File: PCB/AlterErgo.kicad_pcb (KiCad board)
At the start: 2 copper layers, 104 parts, among them J1 GS3, J2 SJ-43514, J3 GS3, J4 Conn_01x02, SW0:10 SW_Push, SW0:11 SW_Push, SW0:12 SW_Push, SW0:7 SW_Push, SW0:8 SW_Push, SW0:9 SW_Push, SW1 SW_SPST, SW1:10 SW_Push, SW1:11 SW_Push, SW1:12 SW_Push, SW1:13 SW_Push, SW1:7 SW_Push, SW1:8 SW_Push, SW1:9 SW_Push, SW2:10 SW_Push, SW2:11 SW_Push, SW2:12 SW_Push, SW2:13 SW_Push, SW2:7 SW_Push, SW2:8 SW_Push, SW2:9 SW_Push, SW3:10 SW_Push, SW3:11 SW_Push, SW3:12 SW_Push, SW3:13 SW_Push, SW3:8 SW_Push, SW3:9 SW_Push, SW4:10 SW_Push, SW4:11 SW_Push, SW4:12 SW_Push, SW4:13 SW_Push, SW4:7 SW_Push, SW4:8 SW_Push, SW4:9 SW_Push, SW5:10 SW_Push, SW5:11 SW_Push, SW5:12 SW_Push, SW5:13 SW_Push, SW5:7 SW_Push, SW5:8 SW_Push, SW5:9 SW_Push, U1 Feather32u4Bluefruit, U2 MCP23018

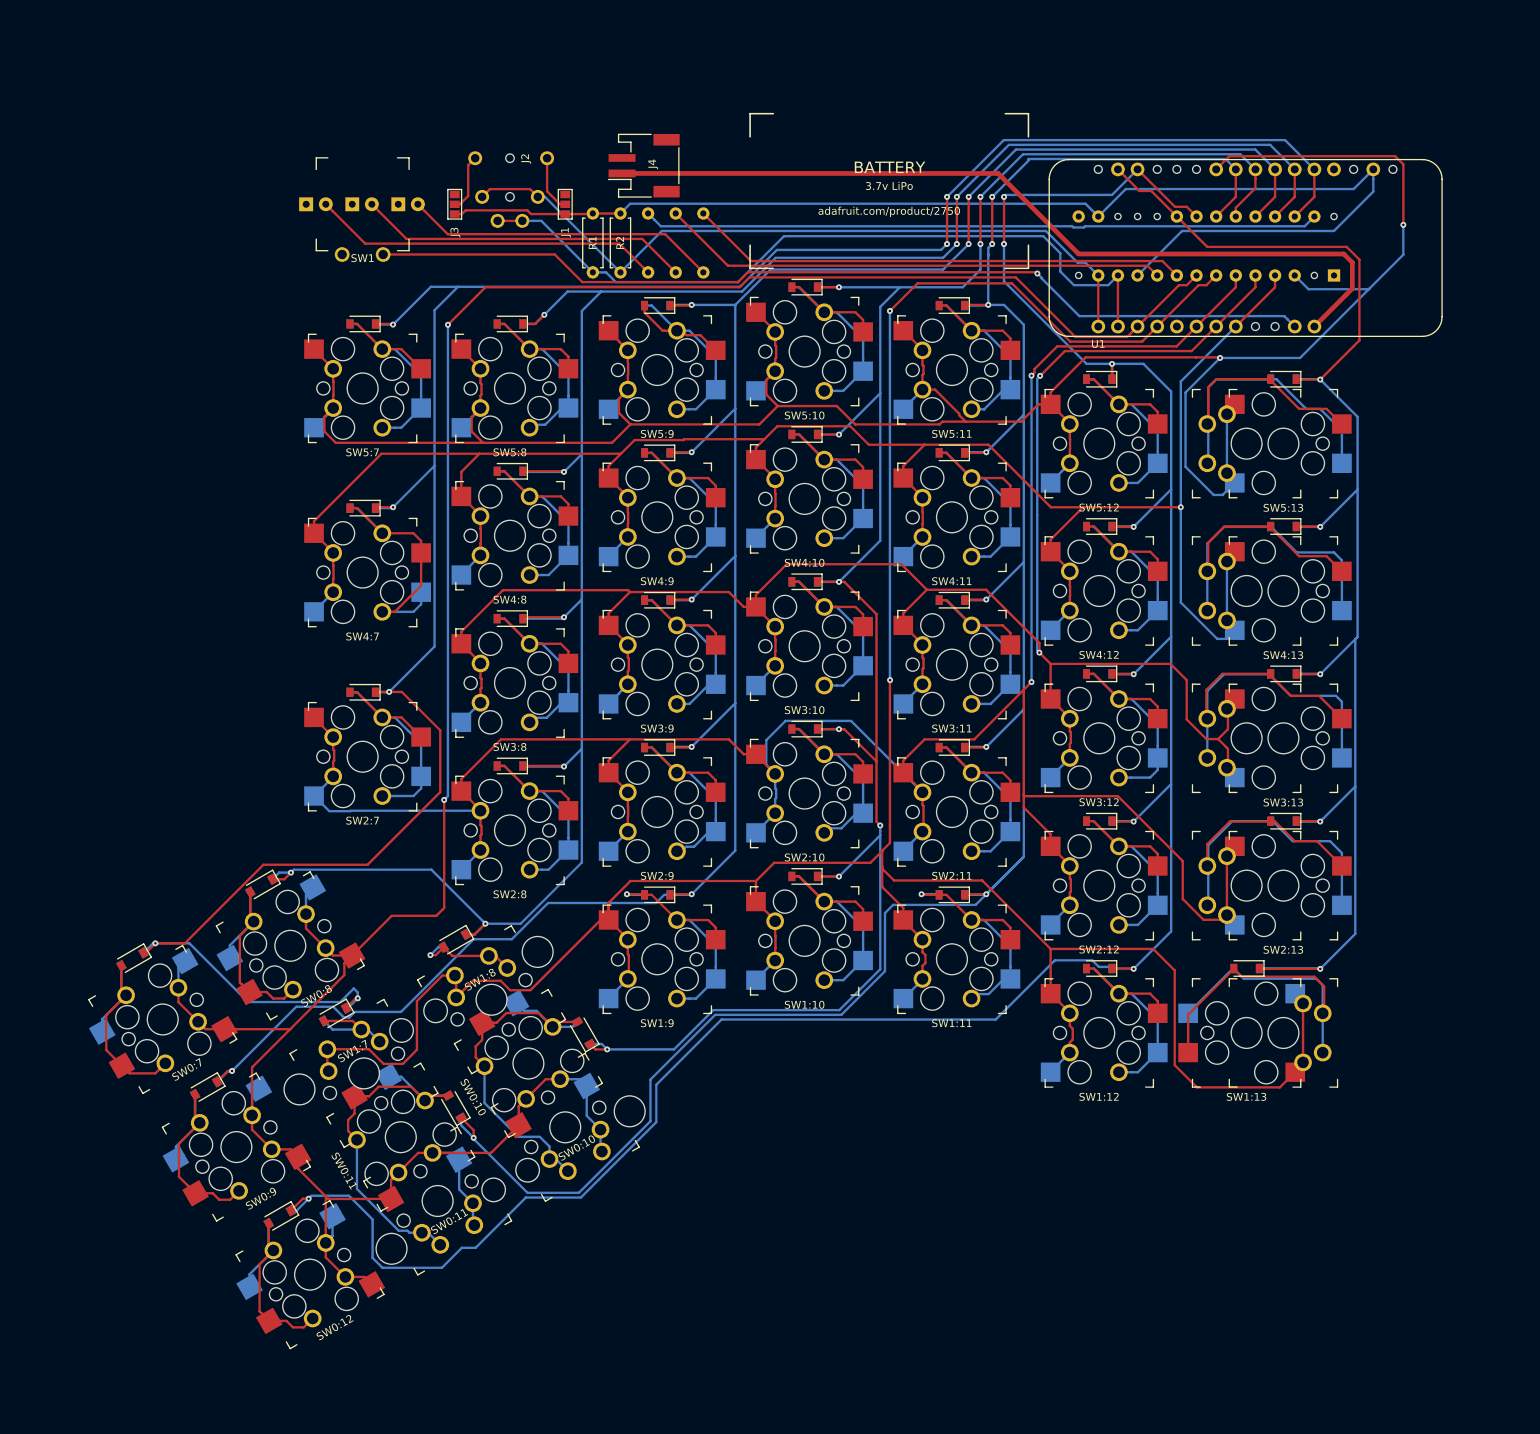
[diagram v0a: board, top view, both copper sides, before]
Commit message: Accept through hole or surface mount 1N4148 diodes; clean up some routing slightly
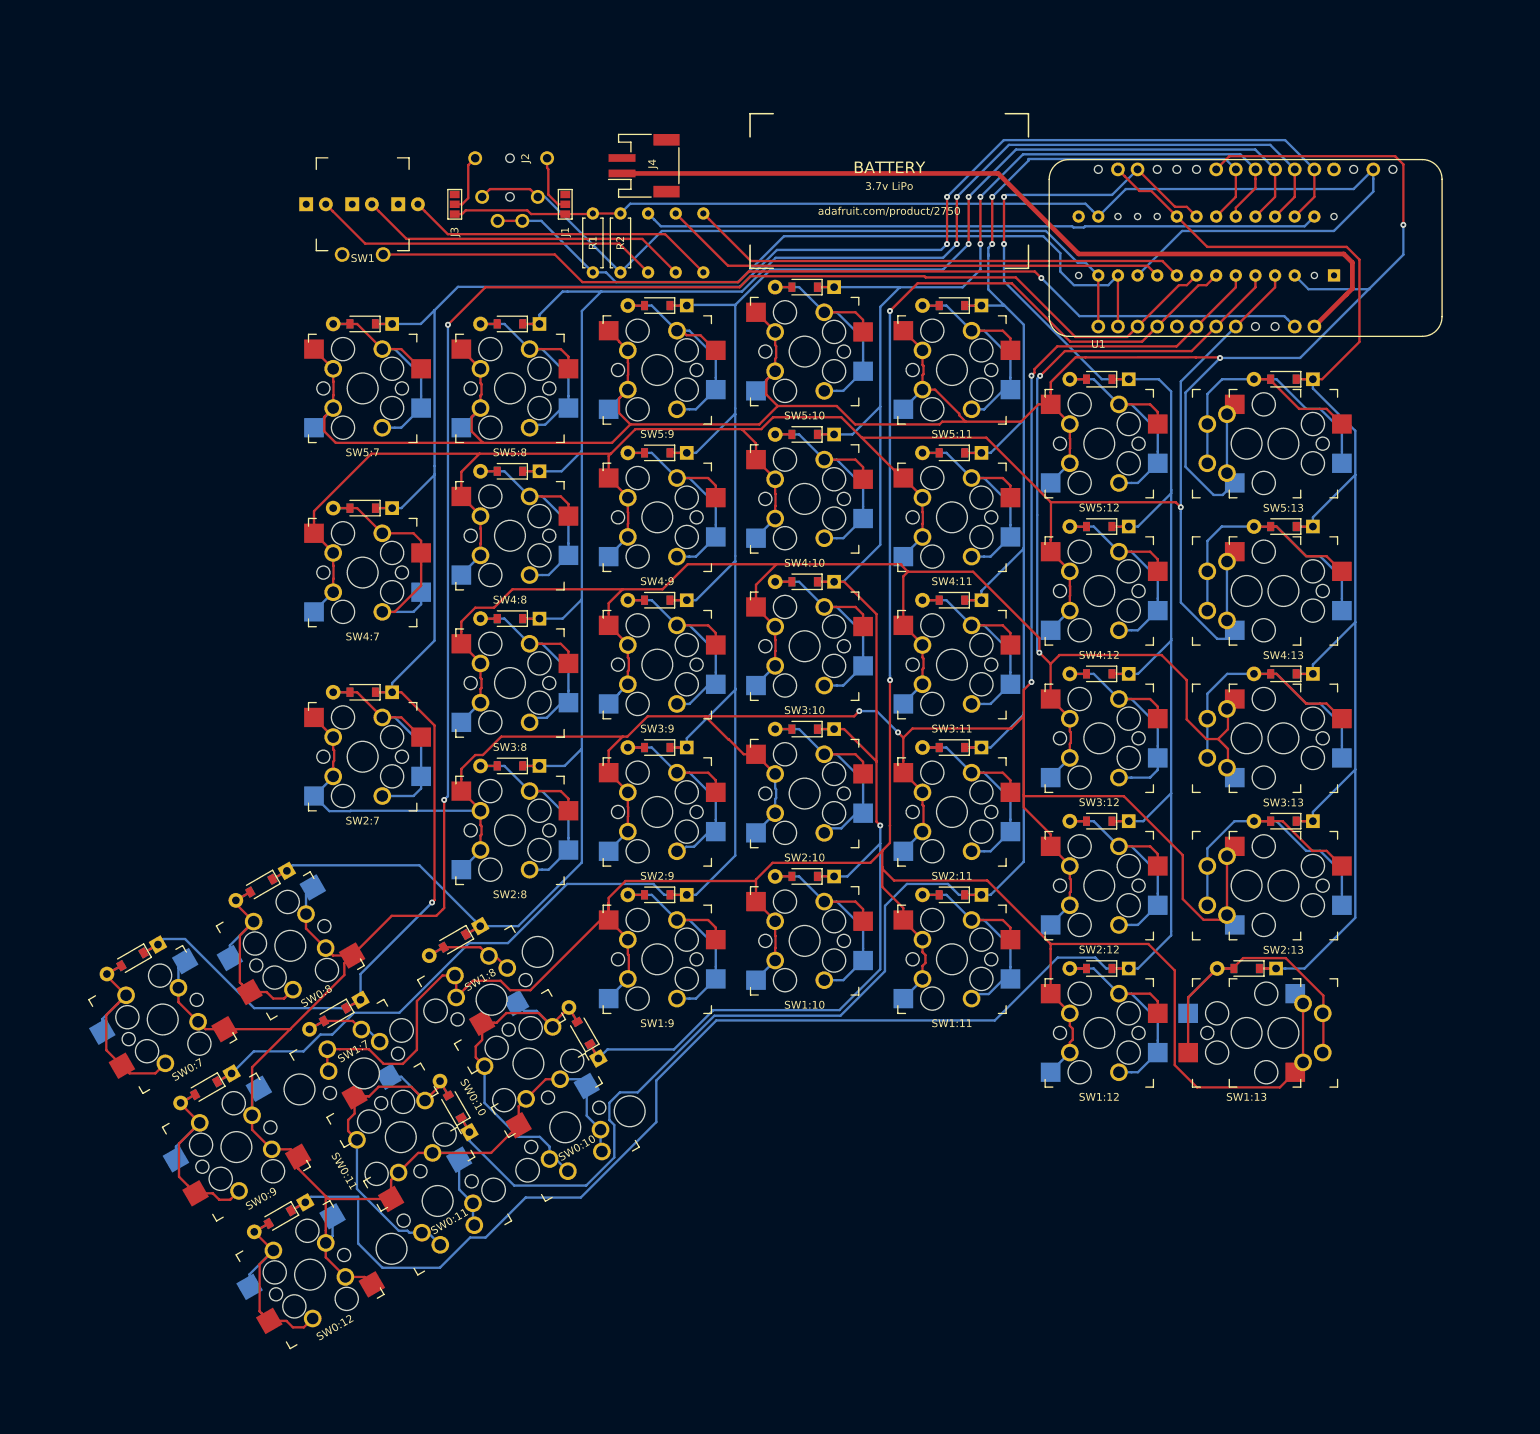
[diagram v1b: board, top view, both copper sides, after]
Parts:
- D0:10, D0:11, D0:12, D0:7, D0:8, D0:9, D1:10, D1:11, D1:12, D1:13, D1:7, D1:8, D1:9, D2:10, D2:11, D2:12, D2:13, D2:7, D2:8, D2:9, D3:10, D3:11, D3:12, D3:13, D3:8, D3:9, D4:10, D4:11, D4:12, D4:13, D4:7, D4:8, D4:9, D5:10, D5:11, D5:12, D5:13, D5:7, D5:8, D5:9: footprint keyboard_accessories:D_SOD-123_2sided_hiddenlabel -> keyboard_accessories:D_SOD-123_2sided_DO-35_combo
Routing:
- net /COL6: track 318.6 -> 297.8 mm, vias 7 -> 3
- net Net-(D1:13-Pad2): track 59.3 -> 46.0 mm
- net Net-(D3:13-Pad2): track 60.4 -> 48.2 mm
- net Net-(D4:13-Pad2): track 60.0 -> 48.3 mm
- net /COL5: track 297.4 -> 285.8 mm, vias 8 -> 2
- net Net-(D2:13-Pad2): track 58.8 -> 47.4 mm
- net Net-(D5:13-Pad2): track 59.1 -> 48.3 mm
- net /COL11: track 292.7 -> 284.4 mm, vias 8 -> 2
- net /ROW3: track 276.8 -> 284.2 mm
- net /COL0: track 194.8 -> 188.4 mm, vias 5 -> 0
- net /ROW4: track 279.7 -> 283.5 mm
- net /COL1: track 327.5 -> 323.8 mm, vias 8 -> 2
- net Net-(D0:11-Pad2): track 49.5 -> 52.4 mm
- net /COL10: track 262.8 -> 260.4 mm, vias 9 -> 3
- net Net-(D0:12-Pad2): track 30.3 -> 32.3 mm
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
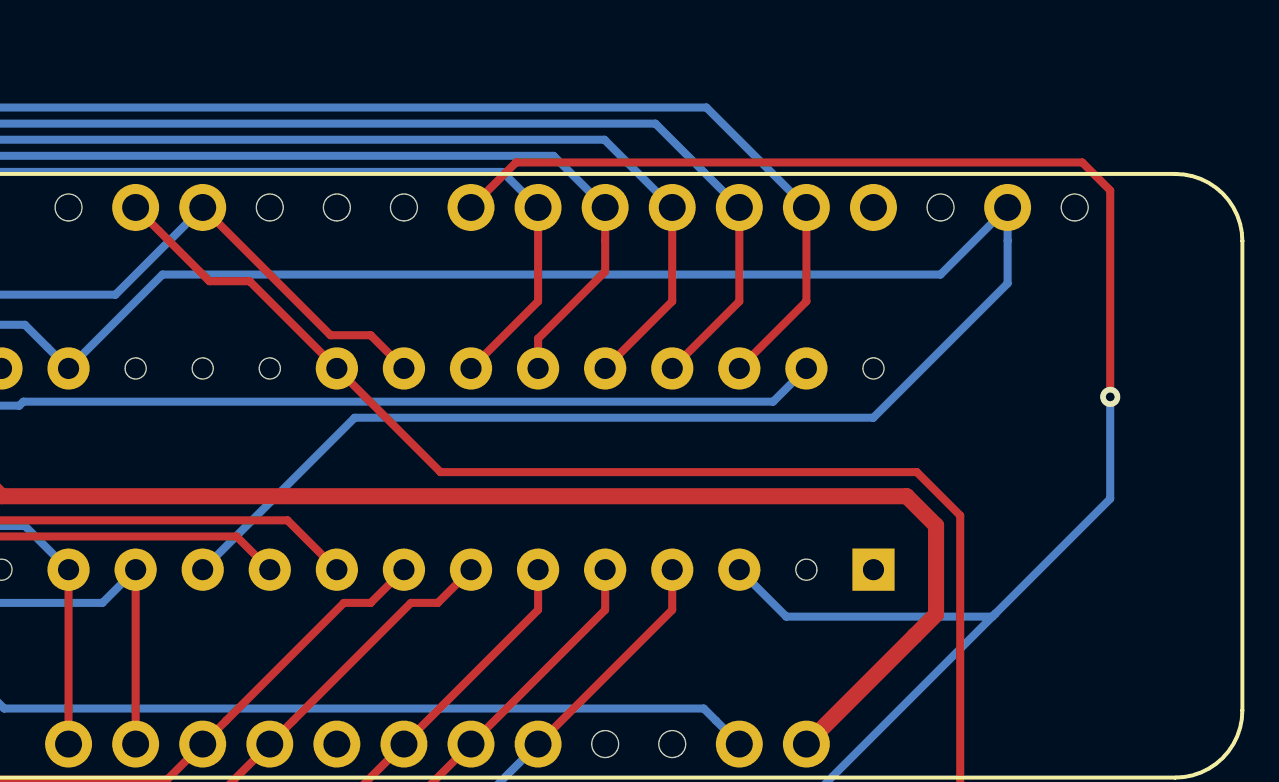
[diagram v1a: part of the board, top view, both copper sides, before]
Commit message: Add hole to allow Feather reset button to be pressed even when installed upside-down on the left-hand PCB
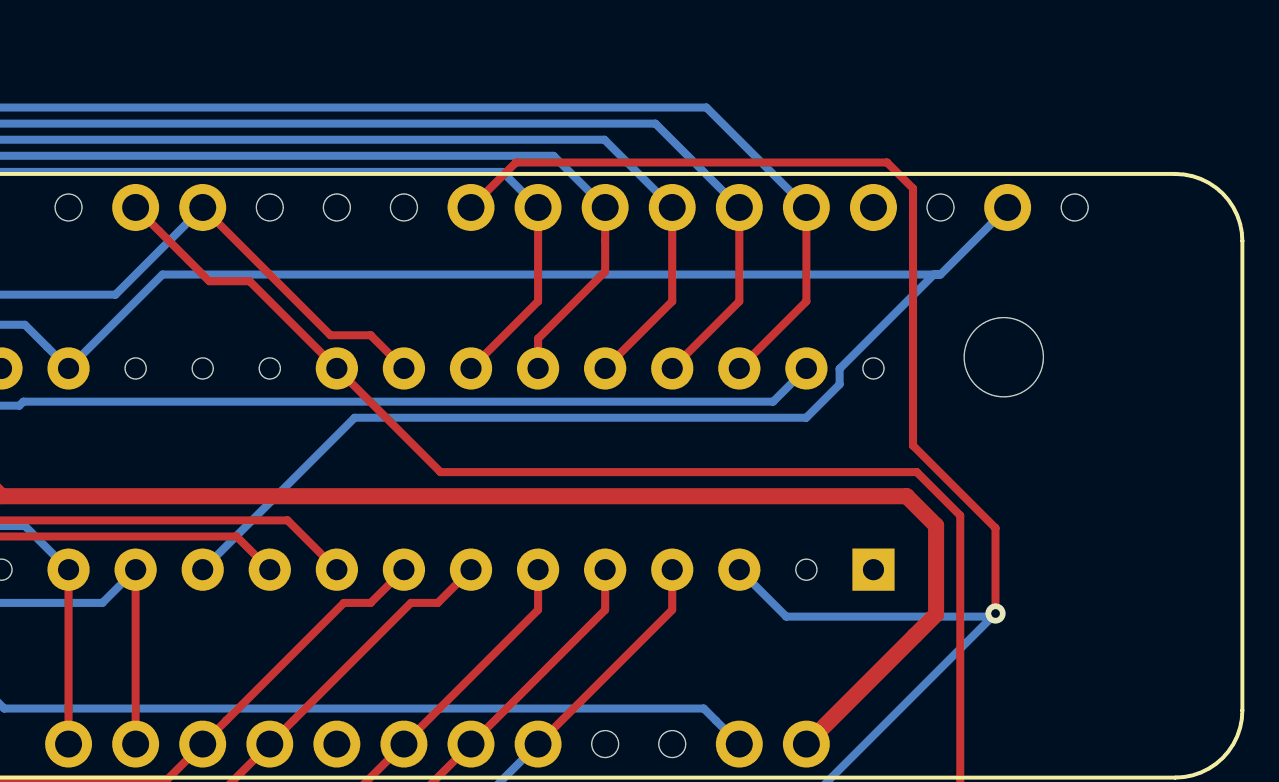
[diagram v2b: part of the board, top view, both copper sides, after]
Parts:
- added RESET: ResetHole, Mounting_Holes:MountingHole_3mm, F.Cu at (211.5, 34.5)
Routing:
- net /ROW5: track 327.3 -> 319.2 mm
- net +3V3: track 160.8 -> 155.7 mm
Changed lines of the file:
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@@
 (kicad_pcb (version 4) (host pcbnew 4.0.7)
   (general
-    (links 546)
-    (no_connects 19)
+    (links 0)
+    (no_connects 15)
     (area 33.589001 -2.08962 221.067701 182.523514)
     (thickness 1.6)
@@
     (tracks 1723)
     (zones 0)
-    (modules 104)
+    (modules 105)
     (nets 69)
   )
@@
     (41 Cmts.User user hide)
     (42 Eco1.User user)
-    (43 Eco2.User user hide)
-    (44 Edge.Cuts user hide)
+    (43 Eco2.User user)
+    (44 Edge.Cuts user)
     (45 Margin user)
     (46 B.CrtYd user)
     (47 F.CrtYd user)
     (48 B.Fab user)
-    (49 F.Fab user hide)
+    (49 F.Fab user)
   )
   (setup
@@
     (mod_text_size 1 1)
     (mod_text_width 0.15)
-    (pad_size 1.02 1.02)
-    (pad_drill 1.02)
+    (pad_size 3 3)
+    (pad_drill 3)
     (pad_to_mask_clearance 0.0508)
     (aux_axis_origin 0 0)
-    (visible_elements FFFFEF7F)
+    (visible_elements FFFFFF7F)
     (pcbplotparams
       (layerselection 0x00030_80000001)
@@
     )
   )
+  (module Mounting_Holes:MountingHole_3mm (layer F.Cu)
+    (at 211.5 34.5)
+    (descr "Mounting Hole 3mm, no annular")
+    (tags "mounting hole 3mm no annular")
+    (attr virtual)
+    (fp_text reference RESET (at 0 -4) (layer Cmts.User) hide
+      (effects (font (size 1 1) (thickness 0.15)))
+    )
+    (fp_text value ResetHole (at 0 4) (layer F.Fab)
+      (effects (font (size 1 1) (thickness 0.15)))
+    )
+    (fp_text user %R (at 0.3 0) (layer F.Fab)
+      (effects (font (size 1 1) (thickness 0.15)))
+    )
+    (fp_circle (center 0 0) (end 3 0) (layer Cmts.User) (width 0.15))
+    (fp_circle (center 0 0) (end 3.25 0) (layer F.CrtYd) (width 0.05))
+    (pad "" np_thru_hole circle (at 0 0) (size 3 3) (drill 3) (layers *.Cu *.Mask))
+  )
   (gr_text SW0:2 (at 92.4375 164.625 30) (layer B.SilkS)
     (effects (font (size 1 1) (thickness 0.15)) (justify mirror))
@@
   (segment (start 198.375 55.959375) (end 196.215 55.959375) (width 0.3048) (layer B.Cu) (net 51))
   (segment (start 196.215 55.959375) (end 198.375 55.959375) (width 0.3048) (layer F.Cu) (net 51))
+  (segment (start 179.6415 31.369) (end 209 31.369) (width 0.3048) (layer B.Cu) (net 52))
+  (segment (start 209 31.369) (end 209.1055 31.369) (width 0.3048) (layer B.Cu) (net 52))
+  (segment (start 186.918689 36.791811) (end 204.019349 36.791809) (width 0.3048) (layer B.Cu) (net 52))
+  (segment (start 204.019349 36.791809) (end 205.282701 35.528457) (width 0.3048) (layer B.Cu) (net 52))
+  (segment (start 205.282701 35.528457) (end 205.282701 34.939141) (width 0.3048) (layer B.Cu) (net 52))
+  (segment (start 205.282701 34.939141) (end 208.852842 31.369) (width 0.3048) (layer B.Cu) (net 52))
+  (segment (start 208.852842 31.369) (end 209 31.369) (width 0.3048) (layer B.Cu) (net 52))
   (segment (start 114.3 34.528125) (end 115.557201 33.270924) (width 0.3048) (layer B.Cu) (net 52))
   (segment (start 115.557201 33.270924) (end 174.431424 33.270924) (width 0.3048) (layer B.Cu) (net 52))
@@
   (segment (start 175.285501 34.125001) (end 176.0855 34.925) (width 0.3048) (layer B.Cu) (net 52))
   (segment (start 181.1655 42.545) (end 186.918689 36.791811) (width 0.3048) (layer B.Cu) (net 52))
-  (segment (start 186.918689 36.791811) (end 206.559347 36.791811) (width 0.3048) (layer B.Cu) (net 52))
-  (segment (start 206.559347 36.791811) (end 211.6455 31.705658) (width 0.3048) (layer B.Cu) (net 52))
-  (segment (start 211.6455 31.705658) (end 211.6455 30.086235) (width 0.3048) (layer B.Cu) (net 52))
-  (segment (start 211.6455 30.086235) (end 211.6455 28.829) (width 0.3048) (layer B.Cu) (net 52))
-  (segment (start 179.6415 31.369) (end 209.1055 31.369) (width 0.3048) (layer B.Cu) (net 52))
   (segment (start 209.1055 31.369) (end 211.6455 28.829) (width 0.3048) (layer B.Cu) (net 52))
   (segment (start 176.0855 34.925) (end 179.6415 31.369) (width 0.3048) (layer B.Cu) (net 52))
@@
   (segment (start 198.9455 42.545) (end 198.9455 44.069) (width 0.3048) (layer F.Cu) (net 65))
   (segment (start 198.9455 44.069) (end 193.8655 49.149) (width 0.3048) (layer F.Cu) (net 65))
+  (via (at 211.1875 44.20493) (size 0.762) (drill 0.3302) (layers F.Cu B.Cu) (net 66))
+  (segment (start 191.3255 28.829) (end 193.0295 27.125) (width 0.3048) (layer F.Cu) (net 66))
+  (segment (start 193.0295 27.125) (end 207.07943 27.125) (width 0.3048) (layer F.Cu) (net 66))
+  (segment (start 207.07943 27.125) (end 208.064101 28.109671) (width 0.3048) (layer F.Cu) (net 66))
+  (segment (start 208.064101 37.846312) (end 211.1875 40.969711) (width 0.3048) (layer F.Cu) (net 66))
+  (segment (start 208.064101 28.109671) (end 208.064101 37.846312) (width 0.3048) (layer F.Cu) (net 66))
+  (segment (start 211.1875 40.969711) (end 211.1875 44.20493) (width 0.3048) (layer F.Cu) (net 66))
   (segment (start 169.9375 56.338017) (end 169.9375 57.64395) (width 0.3048) (layer F.Cu) (net 66))
   (segment (start 169.9375 57.64395) (end 169.9225 57.65895) (width 0.3048) (layer F.Cu) (net 66))
   (segment (start 174.444651 53.136799) (end 173.138718 53.136799) (width 0.3048) (layer F.Cu) (net 66))
   (segment (start 173.138718 53.136799) (end 169.9375 56.338017) (width 0.3048) (layer F.Cu) (net 66))
-  (segment (start 215.531701 36.001761) (end 215.531701 28.182823) (width 0.3048) (layer F.Cu) (net 66))
-  (segment (start 215.531701 28.182823) (end 214.473878 27.125) (width 0.3048) (layer F.Cu) (net 66))
-  (segment (start 214.473878 27.125) (end 193.0295 27.125) (width 0.3048) (layer F.Cu) (net 66))
-  (segment (start 193.0295 27.125) (end 192.671701 27.482799) (width 0.3048) (layer F.Cu) (net 66))
-  (segment (start 192.671701 27.482799) (end 191.3255 28.829) (width 0.3048) (layer F.Cu) (net 66))
-  (segment (start 215.531701 39.860729) (end 211.1875 44.20493) (width 0.3048) (layer B.Cu) (net 66))
   (segment (start 211.1875 44.20493) (end 202.17943 53.213) (width 0.3048) (layer B.Cu) (net 66))
   (segment (start 203.2635 44.323) (end 211.06943 44.323) (width 0.3048) (layer B.Cu) (net 66))
-  (segment (start 211.06943 44.323) (end 211.1875 44.20493) (width 0.3048) (layer B.Cu) (net 66))
-  (segment (start 215.531701 36.001761) (end 215.531701 39.860729) (width 0.3048) (layer B.Cu) (net 66))
   (segment (start 202.17943 53.213) (end 191.8335 53.213) (width 0.3048) (layer B.Cu) (net 66))
   (segment (start 77.1525 54.61) (end 74.6725 52.13) (width 0.3048) (layer F.Cu) (net 66))
@@
   (segment (start 188.709299 53.136799) (end 188.700803 53.128303) (width 0.3048) (layer F.Cu) (net 66))
   (segment (start 169.9225 57.65895) (end 169.9225 59.21375) (width 0.3048) (layer F.Cu) (net 66))
-  (via (at 215.531701 36.001761) (size 0.762) (drill 0.3302) (layers F.Cu B.Cu) (net 66))
   (segment (start 201.4855 42.545) (end 203.2635 44.323) (width 0.3048) (layer B.Cu) (net 66))
   (segment (start 114.503125 29.353125) (end 163.1315 29.353125) (width 0.6096) (layer F.Cu) (net 68))
